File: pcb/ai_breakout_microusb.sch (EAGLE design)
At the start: 2 parts, among them J1 1X04NOSILK

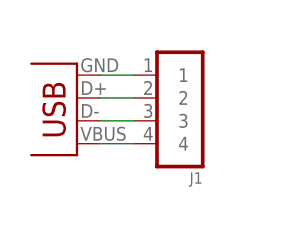
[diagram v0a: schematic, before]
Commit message: redesigned to DIL form factor
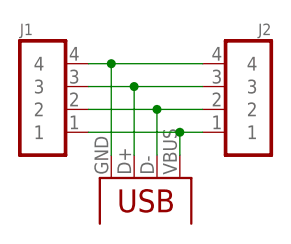
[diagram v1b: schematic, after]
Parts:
- added J2: 1X04NFNS, Ai_Connectors:1X04NFNS
- J1: value 1X04NOSILK -> 1X04NFNS; device Ai_Connectors:1X04NOSILK -> Ai_Connectors:1X04NFNS
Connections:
- net D+: now also J1.3, J2.3; no longer J1.2
- net D-: now also J1.2, J2.2; no longer J1.3
- net GND: now also J1.4, J2.4; no longer J1.1
- net VBUS: now also J1.1, J2.1; no longer J1.4
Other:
- moved on the sheet: J1
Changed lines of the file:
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@@
 <attribute name="REV" value="1.0"/>
 </part>
-<part name="J1" library="Ai_Connectors" deviceset="1X04" device="NOSILK"/>
+<part name="J1" library="Ai_Connectors" deviceset="1X04" device="NFNS" value="1X04NFNS"/>
+<part name="J2" library="Ai_Connectors" deviceset="1X04" device="NFNS" value="1X04NFNS"/>
 <part name="USB1" library="Ai_Connectors" deviceset="USB" device="MICROB-TH"/>
 </parts>
@@
 <instance part="FRAME1" gate="G$1" x="0" y="0"/>
 <instance part="FRAME1" gate="G$2" x="147.32" y="0"/>
-<instance part="J1" gate="G$1" x="140.97" y="99.06" rot="R180"/>
-<instance part="USB1" gate="G$1" x="125.73" y="100.33" rot="R180"/>
+<instance part="J1" gate="G$1" x="125.73" y="102.87"/>
+<instance part="J2" gate="G$1" x="148.59" y="102.87" rot="MR0"/>
+<instance part="USB1" gate="G$1" x="137.16" y="88.9" rot="R270"/>
 </instances>
 <busses>
 </busses>
 <nets>
-<net name="D+" class="0">
+<net name="VBUS" class="0">
 <segment>
-<pinref part="J1" gate="G$1" pin="2"/>
-<pinref part="USB1" gate="G$1" pin="D+"/>
-<wire x1="132.08" y1="101.6" x2="135.89" y2="101.6" width="0.1524" layer="91"/>
+<pinref part="USB1" gate="G$1" pin="VBUS"/>
+<wire x1="140.97" y1="95.25" x2="140.97" y2="97.79" width="0.1524" layer="91"/>
+<pinref part="J2" gate="G$1" pin="1"/>
+<wire x1="140.97" y1="97.79" x2="143.51" y2="97.79" width="0.1524" layer="91"/>
+<pinref part="J1" gate="G$1" pin="1"/>
+<wire x1="130.81" y1="97.79" x2="140.97" y2="97.79" width="0.1524" layer="91"/>
+<junction x="140.97" y="97.79"/>
 </segment>
 </net>
 <net name="D-" class="0">
 <segment>
-<pinref part="J1" gate="G$1" pin="3"/>
 <pinref part="USB1" gate="G$1" pin="D-"/>
-<wire x1="132.08" y1="99.06" x2="135.89" y2="99.06" width="0.1524" layer="91"/>
-</segment>
-</net>
-<net name="VBUS" class="0">
-<segment>
-<pinref part="J1" gate="G$1" pin="4"/>
-<pinref part="USB1" gate="G$1" pin="VBUS"/>
-<wire x1="132.08" y1="96.52" x2="135.89" y2="96.52" width="0.1524" layer="91"/>
+<wire x1="138.43" y1="95.25" x2="138.43" y2="100.33" width="0.1524" layer="91"/>
+<pinref part="J2" gate="G$1" pin="2"/>
+<wire x1="138.43" y1="100.33" x2="143.51" y2="100.33" width="0.1524" layer="91"/>
+<pinref part="J1" gate="G$1" pin="2"/>
+<wire x1="130.81" y1="100.33" x2="138.43" y2="100.33" width="0.1524" layer="91"/>
+<junction x="138.43" y="100.33"/>
 </segment>
 </net>
 <net name="GND" class="0">
 <segment>
-<pinref part="J1" gate="G$1" pin="1"/>
+<pinref part="J1" gate="G$1" pin="4"/>
+<wire x1="130.81" y1="105.41" x2="133.35" y2="105.41" width="0.1524" layer="91"/>
 <pinref part="USB1" gate="G$1" pin="GND"/>
-<wire x1="132.08" y1="104.14" x2="135.89" y2="104.14" width="0.1524" layer="91"/>
+<wire x1="133.35" y1="105.41" x2="133.35" y2="95.25" width="0.1524" layer="91"/>
+<pinref part="J2" gate="G$1" pin="4"/>
+<wire x1="133.35" y1="105.41" x2="143.51" y2="105.41" width="0.1524" layer="91"/>
+<junction x="133.35" y="105.41"/>
 </segment>
 </net>
+<net name="D+" class="0">
+<segment>
+<pinref part="J2" gate="G$1" pin="3"/>
+<pinref part="USB1" gate="G$1" pin="D+"/>
+<wire x1="143.51" y1="102.87" x2="135.89" y2="102.87" width="0.1524" layer="91"/>
+<wire x1="135.89" y1="102.87" x2="135.89" y2="95.25" width="0.1524" layer="91"/>
+<pinref part="J1" gate="G$1" pin="3"/>
+<wire x1="135.89" y1="102.87" x2="130.81" y2="102.87" width="0.1524" layer="91"/>
+<junction x="135.89" y="102.87"/>
+</segment>
+</net>

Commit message: ready for manufacturing
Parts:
- added U$2: AI-LOGOXS, Ai_Miscellany:AI-LOGOXS
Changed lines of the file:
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@@
 <part name="J2" library="Ai_Connectors" deviceset="1X04" device="NFNS" value="1X04NFNS"/>
 <part name="USB1" library="Ai_Connectors" deviceset="USB" device="MICROB-TH"/>
+<part name="U$2" library="Ai_Miscellany" deviceset="AI-LOGO" device="XS"/>
 </parts>
 <sheets>
@@
 <instance part="J2" gate="G$1" x="148.59" y="102.87" rot="MR0"/>
 <instance part="USB1" gate="G$1" x="137.16" y="88.9" rot="R270"/>
+<instance part="U$2" gate="G$1" x="139.7" y="16.51"/>
 </instances>
 <busses>

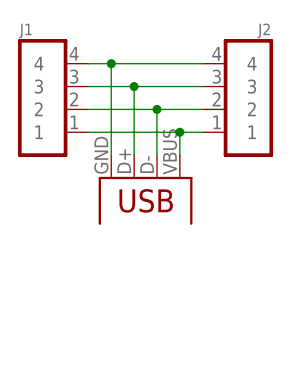
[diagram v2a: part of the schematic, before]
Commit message: udpated to 2-pin version
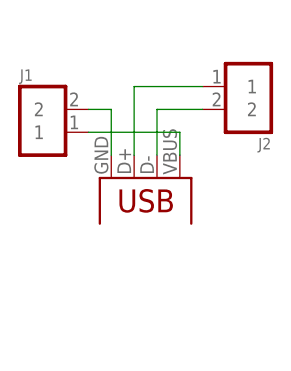
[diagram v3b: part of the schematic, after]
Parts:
- J1: value 1X04NFNS -> 1X02; device Ai_Connectors:1X04NFNS -> Ai_Connectors:1X02
- J2: value 1X04NFNS -> 1X02NOFIRST; device Ai_Connectors:1X04NFNS -> Ai_Connectors:1X02NOFIRST
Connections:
- net D+: now also J2.1; no longer J1.3, J2.3
- net D-: no longer J1.2
- net GND: now also J1.2; no longer J1.4, J2.4
- net VBUS: no longer J2.1
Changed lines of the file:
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@@
 <?xml version="1.0" encoding="utf-8"?>
 <!DOCTYPE eagle SYSTEM "eagle.dtd">
-<eagle version="7.1.0">
+<eagle version="6.5.0">
 <drawing>
 <settings>
@@
 <attribute name="REV" value="1.0"/>
 </part>
-<part name="J1" library="Ai_Connectors" deviceset="1X04" device="NFNS" value="1X04NFNS"/>
-<part name="J2" library="Ai_Connectors" deviceset="1X04" device="NFNS" value="1X04NFNS"/>
 <part name="USB1" library="Ai_Connectors" deviceset="USB" device="MICROB-TH"/>
 <part name="U$2" library="Ai_Miscellany" deviceset="AI-LOGO" device="XS"/>
+<part name="J1" library="Ai_Connectors" deviceset="1X02" device=""/>
+<part name="J2" library="Ai_Connectors" deviceset="1X02" device="NOFIRST" value="1X02NOFIRST"/>
 </parts>
 <sheets>
@@
 <instance part="FRAME1" gate="G$1" x="0" y="0"/>
 <instance part="FRAME1" gate="G$2" x="147.32" y="0"/>
-<instance part="J1" gate="G$1" x="125.73" y="102.87"/>
-<instance part="J2" gate="G$1" x="148.59" y="102.87" rot="MR0"/>
 <instance part="USB1" gate="G$1" x="137.16" y="88.9" rot="R270"/>
 <instance part="U$2" gate="G$1" x="139.7" y="16.51"/>
+<instance part="J1" gate="G$1" x="125.73" y="100.33"/>
+<instance part="J2" gate="G$1" x="148.59" y="100.33" rot="R180"/>
 </instances>
 <busses>
@@
 <pinref part="USB1" gate="G$1" pin="VBUS"/>
 <wire x1="140.97" y1="95.25" x2="140.97" y2="97.79" width="0.1524" layer="91"/>
-<pinref part="J2" gate="G$1" pin="1"/>
-<wire x1="140.97" y1="97.79" x2="143.51" y2="97.79" width="0.1524" layer="91"/>
+<wire x1="140.97" y1="97.79" x2="130.81" y2="97.79" width="0.1524" layer="91"/>
 <pinref part="J1" gate="G$1" pin="1"/>
-<wire x1="130.81" y1="97.79" x2="140.97" y2="97.79" width="0.1524" layer="91"/>
-<junction x="140.97" y="97.79"/>
 </segment>
 </net>
@@
 <pinref part="USB1" gate="G$1" pin="D-"/>
 <wire x1="138.43" y1="95.25" x2="138.43" y2="100.33" width="0.1524" layer="91"/>
+<wire x1="138.43" y1="100.33" x2="143.51" y2="100.33" width="0.1524" layer="91"/>
 <pinref part="J2" gate="G$1" pin="2"/>
-<wire x1="138.43" y1="100.33" x2="143.51" y2="100.33" width="0.1524" layer="91"/>
+</segment>
+</net>
+<net name="GND" class="0">
+<segment>
+<wire x1="130.81" y1="100.33" x2="133.35" y2="100.33" width="0.1524" layer="91"/>
+<pinref part="USB1" gate="G$1" pin="GND"/>
+<wire x1="133.35" y1="100.33" x2="133.35" y2="95.25" width="0.1524" layer="91"/>
 <pinref part="J1" gate="G$1" pin="2"/>
-<wire x1="130.81" y1="100.33" x2="138.43" y2="100.33" width="0.1524" layer="91"/>
-<junction x="138.43" y="100.33"/>
-</segment>
-</net>
-<net name="GND" class="0">
-<segment>
-<pinref part="J1" gate="G$1" pin="4"/>
-<wire x1="130.81" y1="105.41" x2="133.35" y2="105.41" width="0.1524" layer="91"/>
-<pinref part="USB1" gate="G$1" pin="GND"/>
-<wire x1="133.35" y1="105.41" x2="133.35" y2="95.25" width="0.1524" layer="91"/>
-<pinref part="J2" gate="G$1" pin="4"/>
-<wire x1="133.35" y1="105.41" x2="143.51" y2="105.41" width="0.1524" layer="91"/>
-<junction x="133.35" y="105.41"/>
 </segment>
 </net>
 <net name="D+" class="0">
 <segment>
-<pinref part="J2" gate="G$1" pin="3"/>
 <pinref part="USB1" gate="G$1" pin="D+"/>
-<wire x1="143.51" y1="102.87" x2="135.89" y2="102.87" width="0.1524" layer="91"/>
 <wire x1="135.89" y1="102.87" x2="135.89" y2="95.25" width="0.1524" layer="91"/>
-<pinref part="J1" gate="G$1" pin="3"/>
-<wire x1="135.89" y1="102.87" x2="130.81" y2="102.87" width="0.1524" layer="91"/>
-<junction x="135.89" y="102.87"/>
-</segment>
-</net>
+<wire x1="135.89" y1="102.87" x2="143.51" y2="102.87" width="0.1524" layer="91"/>
+<pinref part="J2" gate="G$1" pin="1"/>
+</segment>
+</net>
